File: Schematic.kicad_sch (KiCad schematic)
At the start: 118 parts, among them J1 Screw_Terminal_01x04, J20 T44007, J21 T44007, Q1 HY1707, Q20 BC817, Q21 SUD50P06-15, U1 UC3845, U20 TCMT1108, U21 TL431M

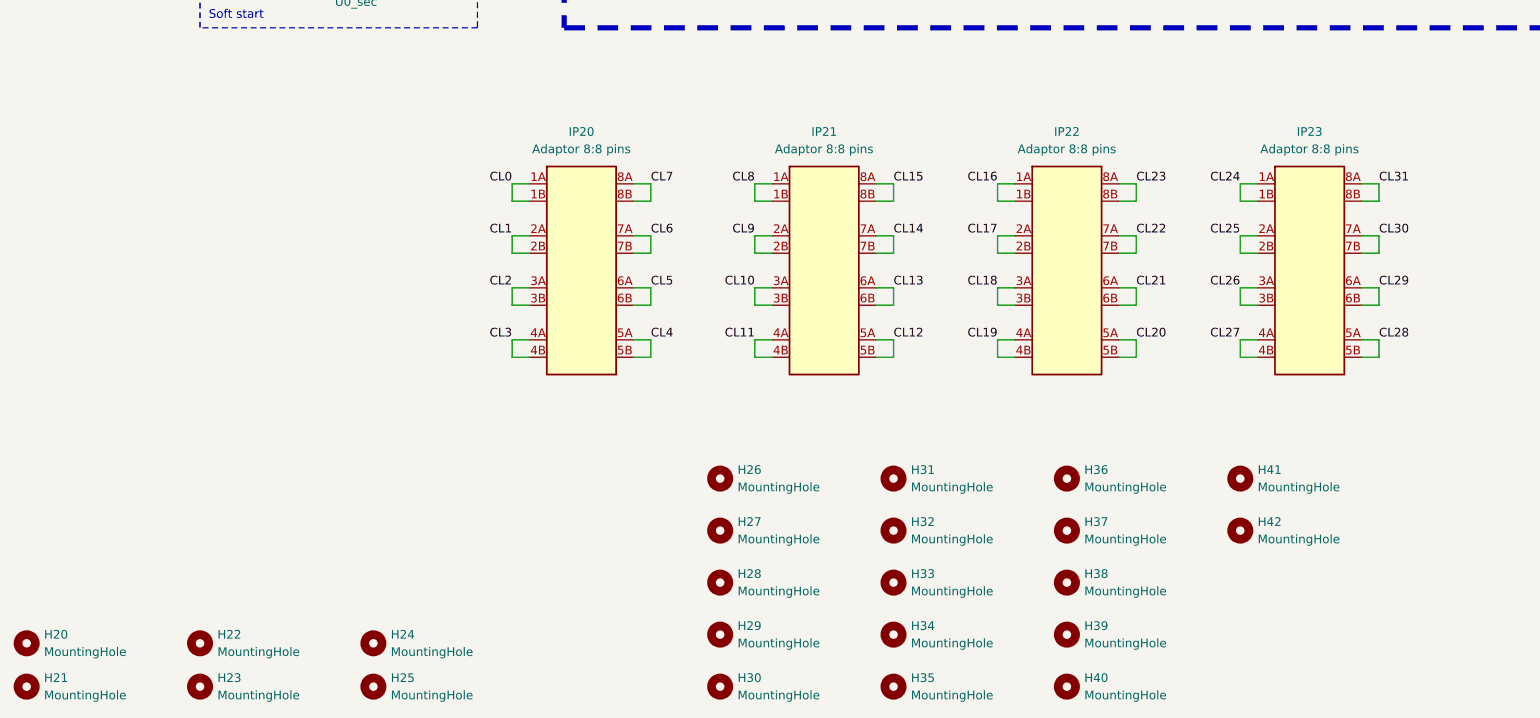
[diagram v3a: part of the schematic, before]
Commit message: Removed extra prototyping area and started updating mfg docs
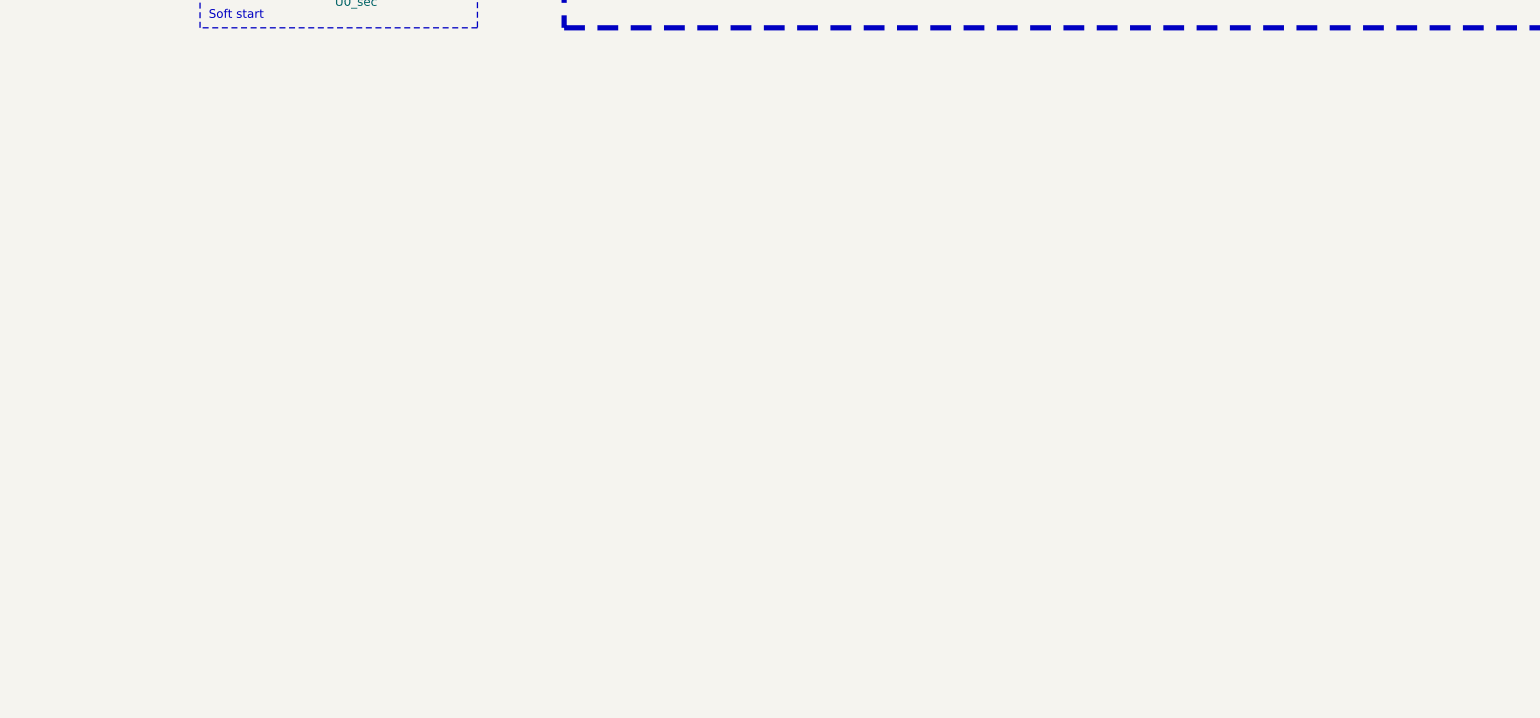
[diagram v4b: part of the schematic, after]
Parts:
- removed H20, H21, H22, H23, H24, H25: MountingHole, MountingHole:MountingHole_3.2mm_M3, symbol Mechanical:MountingHole
- removed H26: MountingHole, Personal:Hole_0.3mm, symbol Mechanical:MountingHole
- removed H27: MountingHole, Personal:Hole_0.4mm, symbol Mechanical:MountingHole
- removed H28: MountingHole, Personal:Hole_0.5mm, symbol Mechanical:MountingHole
- removed H29: MountingHole, Personal:Hole_0.6mm, symbol Mechanical:MountingHole
- removed H30: MountingHole, Personal:Hole_0.7mm, symbol Mechanical:MountingHole
- removed H31: MountingHole, Personal:Hole_0.8mm, symbol Mechanical:MountingHole
- removed H32: MountingHole, Personal:Hole_0.9mm, symbol Mechanical:MountingHole
- removed H33: MountingHole, Personal:Hole_1.0mm, symbol Mechanical:MountingHole
- removed H34: MountingHole, Personal:Hole_1.2mm, symbol Mechanical:MountingHole
- removed H35: MountingHole, Personal:Hole_1.4mm, symbol Mechanical:MountingHole
- removed H36: MountingHole, Personal:Hole_1.6mm, symbol Mechanical:MountingHole
- removed H37: MountingHole, Personal:Hole_1.8mm, symbol Mechanical:MountingHole
- removed H38: MountingHole, Personal:Hole_2.0mm, symbol Mechanical:MountingHole
- removed H39: MountingHole, Personal:Hole_2.5mm, symbol Mechanical:MountingHole
- removed H40: MountingHole, Personal:Hole_3.0mm, symbol Mechanical:MountingHole
- removed H41: MountingHole, Personal:Hole_3.5mm, symbol Mechanical:MountingHole
- removed H42: MountingHole, Personal:Hole_4.0mm, symbol Mechanical:MountingHole
- removed IP20, IP21, IP22, IP23: Adaptor 8:8 pins, Personal:Soic-8_to_DIP-8, symbol personal:Adaptor_8_to_8
